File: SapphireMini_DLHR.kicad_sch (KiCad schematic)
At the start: 17 parts, among them IC201 DLHR-F50D-E1BD-C-NAV8, U201 LIS331DLHTR, U202 BMP390, U203 MS5525DSO

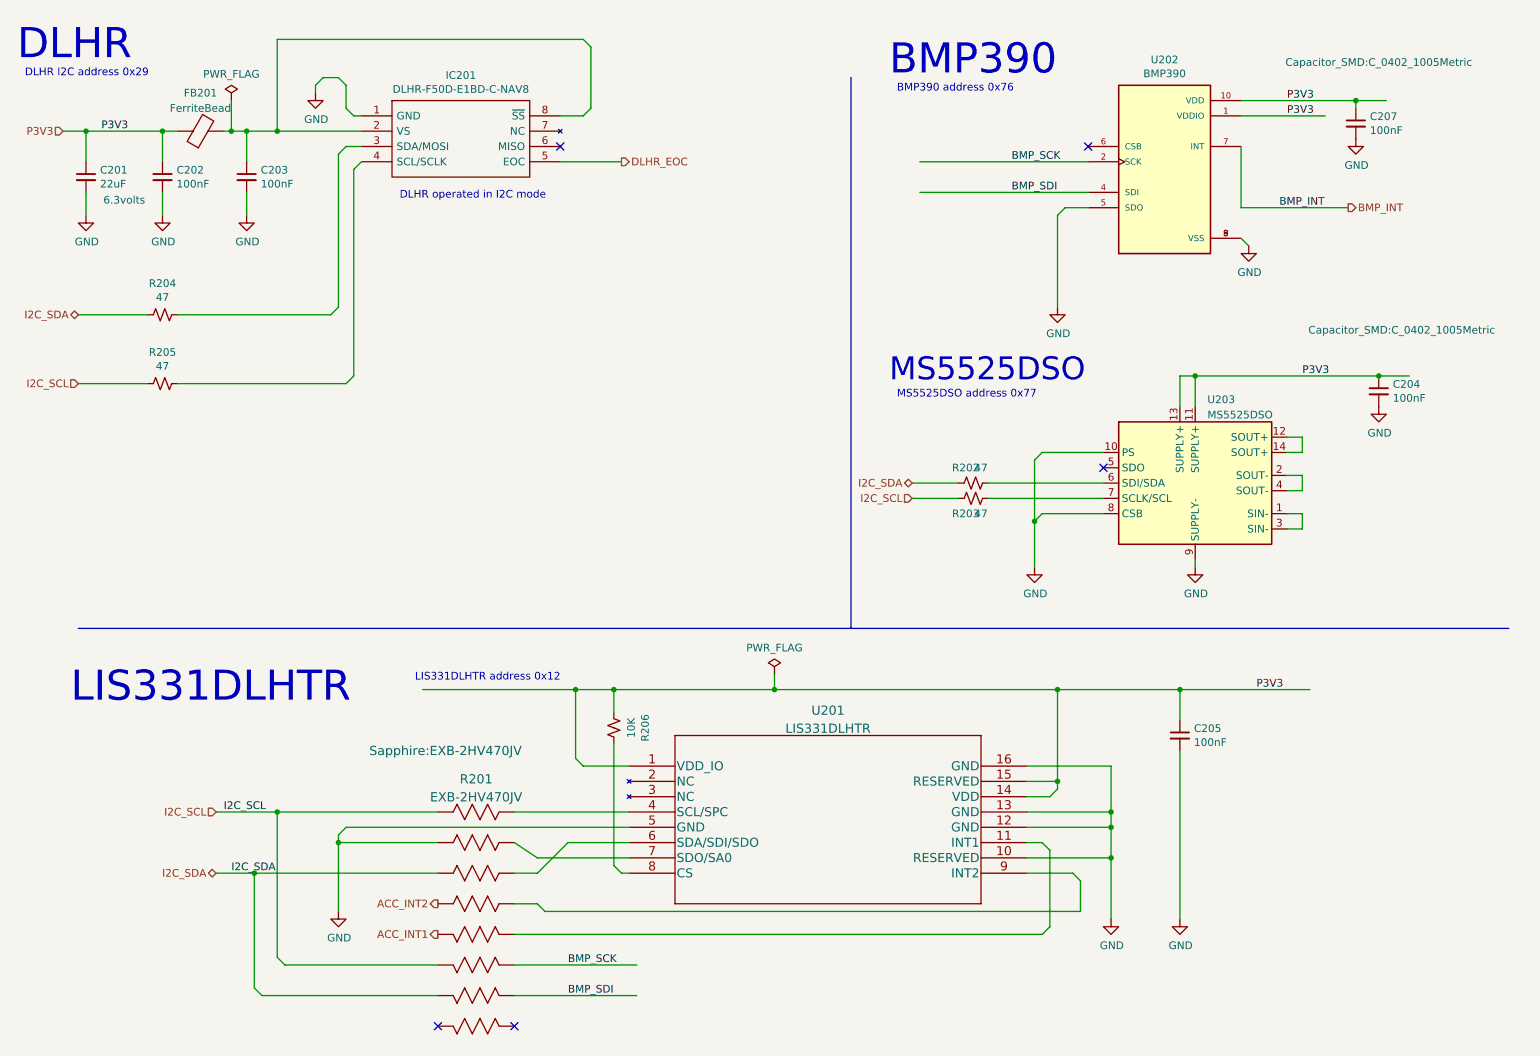
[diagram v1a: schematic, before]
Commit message: updated new layout - no routing
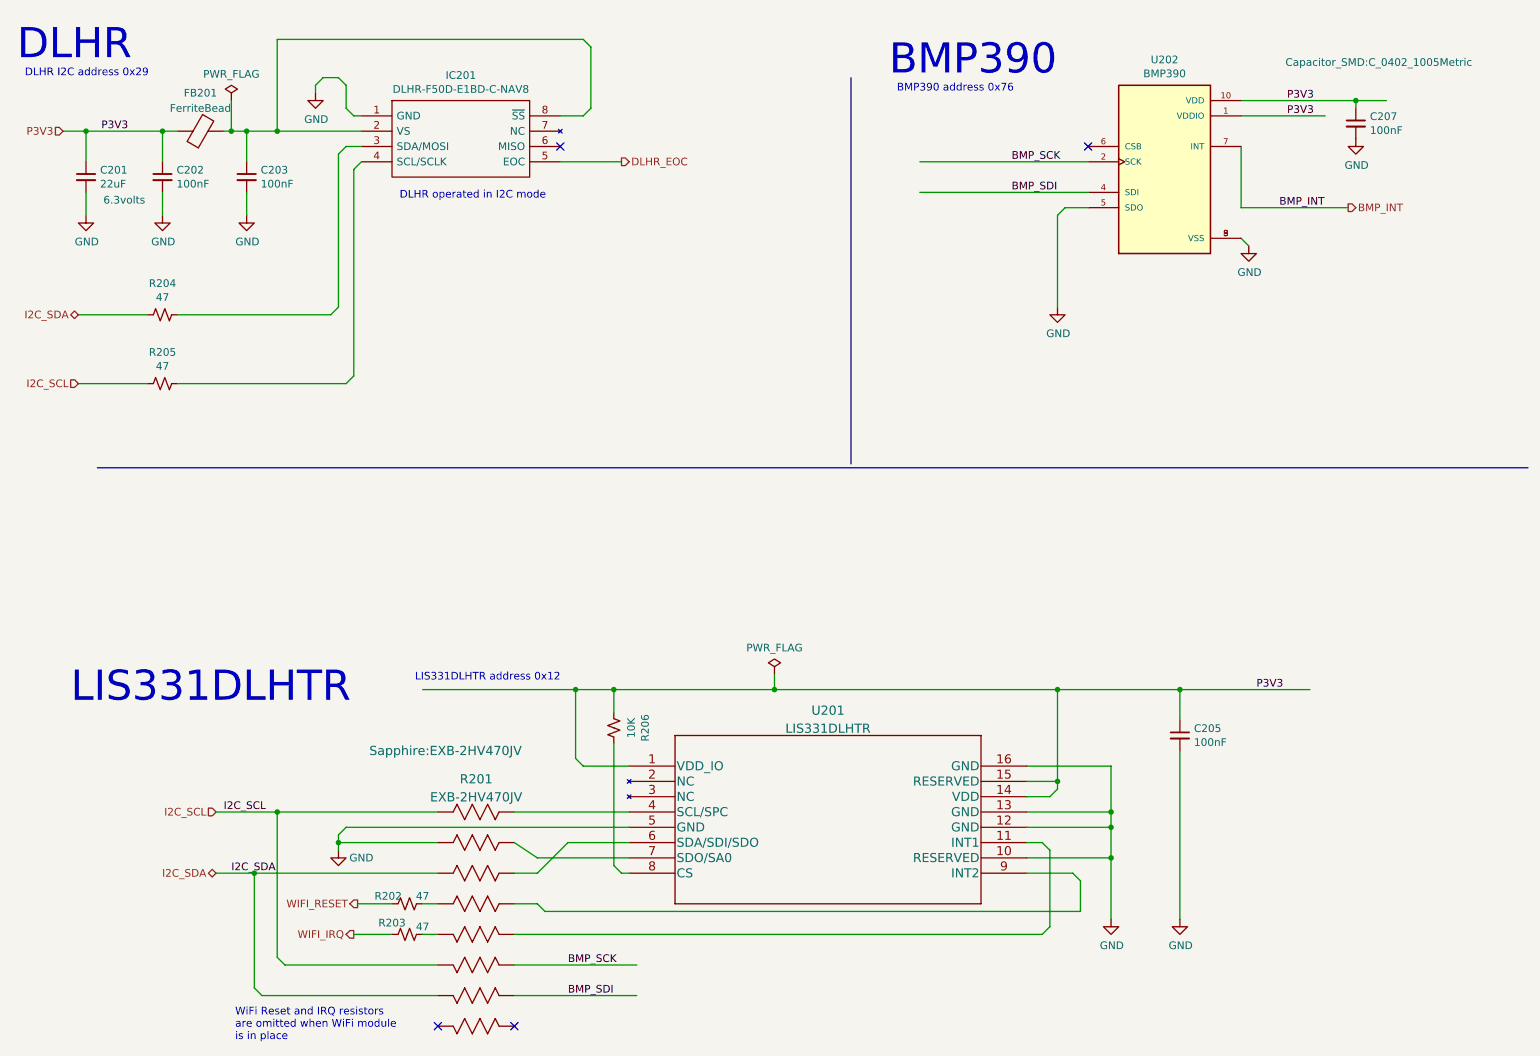
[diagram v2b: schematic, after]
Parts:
- removed C204: 100nF, Capacitor_SMD:C_0402_1005Metric, symbol Device:C_Small
- removed U203: MS5525DSO, Sapphire:TE_5525DSO-DB001DS, symbol Sensor_Pressure:MS5525DSO
- R201: symbol PanasonicRA:EXB-2HV470JV -> sapphireMini:EXB-2HV470JV_1
- U202: symbol BMP388:BMP388 -> sapphireMini:BMP388; MANUFACTURER (none) -> BOSCH
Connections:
- net ACC_INT1 is gone; now on an unnamed net: R201.5
- net ACC_INT2 is gone; now on an unnamed net: R201.4
- net I2C_SCL: no longer R203.2
- net I2C_SDA: no longer R202.2
- new net WIFI_IRQ: R203.2
- new net WIFI_RESET: R202.2
- no-connect marks 5 -> 4
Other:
- note added: "WiFi Reset and IRQ resistors are omitted when WiFi module is in place"
- note removed: "MS5525DSO"
- note removed: "MS5525DSO address 0x77"

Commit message: 6 Layer Routing
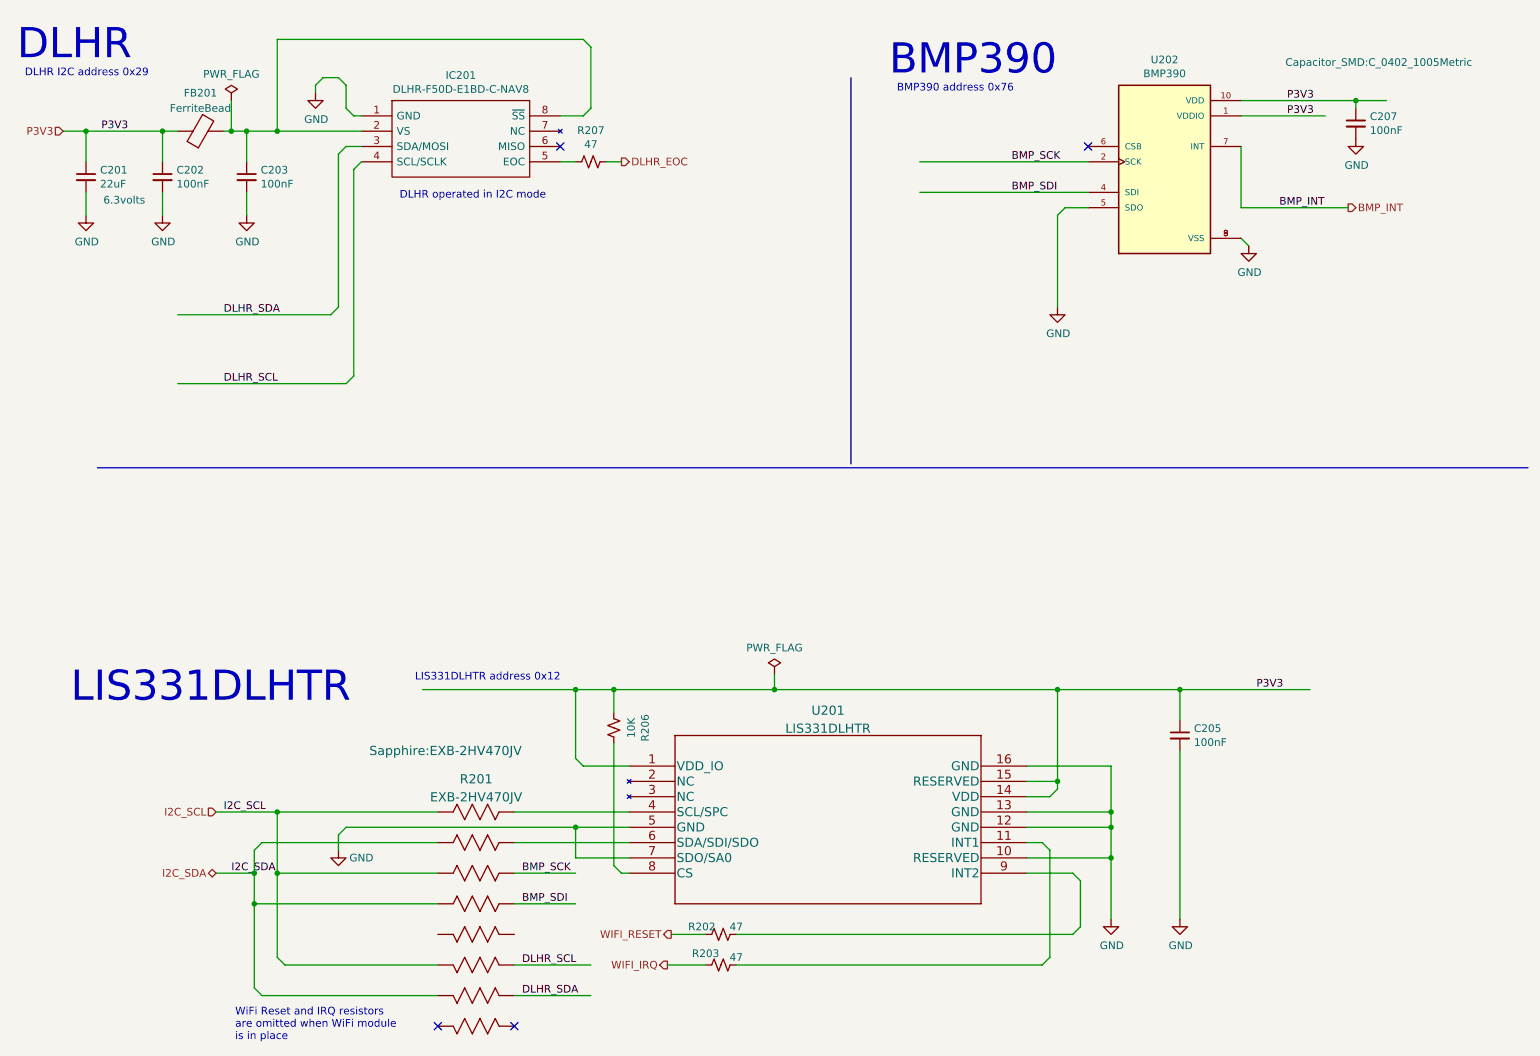
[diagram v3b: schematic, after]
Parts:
- removed R204, R205: 47, Resistor_SMD:R_0603_1608Metric, symbol Device:R_Small_US
- added R207: 47, Resistor_SMD:R_0603_1608Metric, symbol Device:R_Small_US
- FB201: footprint Inductor_SMD:L_0201_0603Metric -> Inductor_SMD:L_0603_1608Metric
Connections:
- net BMP_SCK: now also R201.14; no longer R201.11
- net BMP_SDI: now also R201.13; no longer R201.10
- net DLHR_EOC: now also R207.1; no longer IC201.5 (EOC)
- net GND: now also U201.7 (SDO/SA0); no longer R201.2
- net I2C_SCL: now also R201.3
- net I2C_SDA: now also R201.2, R201.4; no longer R201.3
- net DLHR_SDA: now reaches IC201.3 (SDA/MOSI)
- net DLHR_SDA: now also R201.10
- net DLHR_SCL: now reaches IC201.4 (SCL/SCLK)
- net DLHR_SCL: now also R201.11
- net at R201.12: no longer U201.11 (INT1)
- net at U201.9 (INT2): now also R202.1; no longer R201.13
- net at U201.6 (SDA/SDI/SDO): now also R201.15; no longer R201.14
- net at R201.5: no longer R203.1
- new net: IC201.5 (EOC), R207.2
- new net: R203.1, U201.11 (INT1)
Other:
- moved on the sheet: R202, R203

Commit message: Added optional RSCK footprint
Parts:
- C201: Attrition (none) -> 0
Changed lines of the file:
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@@
+      (effects (font (size 1.27 1.27)) hide)
+    )
+    (property "Attrition" "0" (id 17) (at 27.94 41.91 0)
       (effects (font (size 1.27 1.27)) hide)
     )

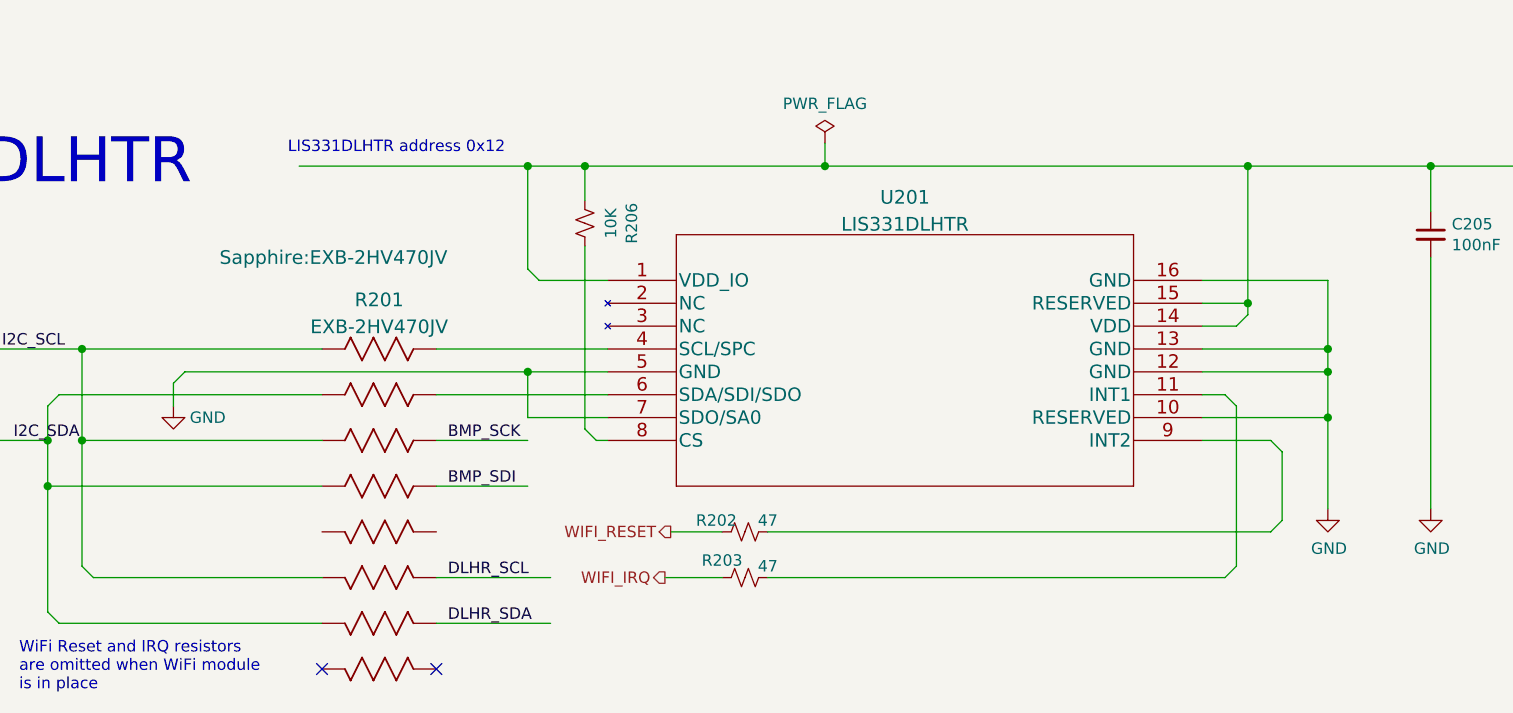
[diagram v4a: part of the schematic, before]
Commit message: Updated to fix noted problems
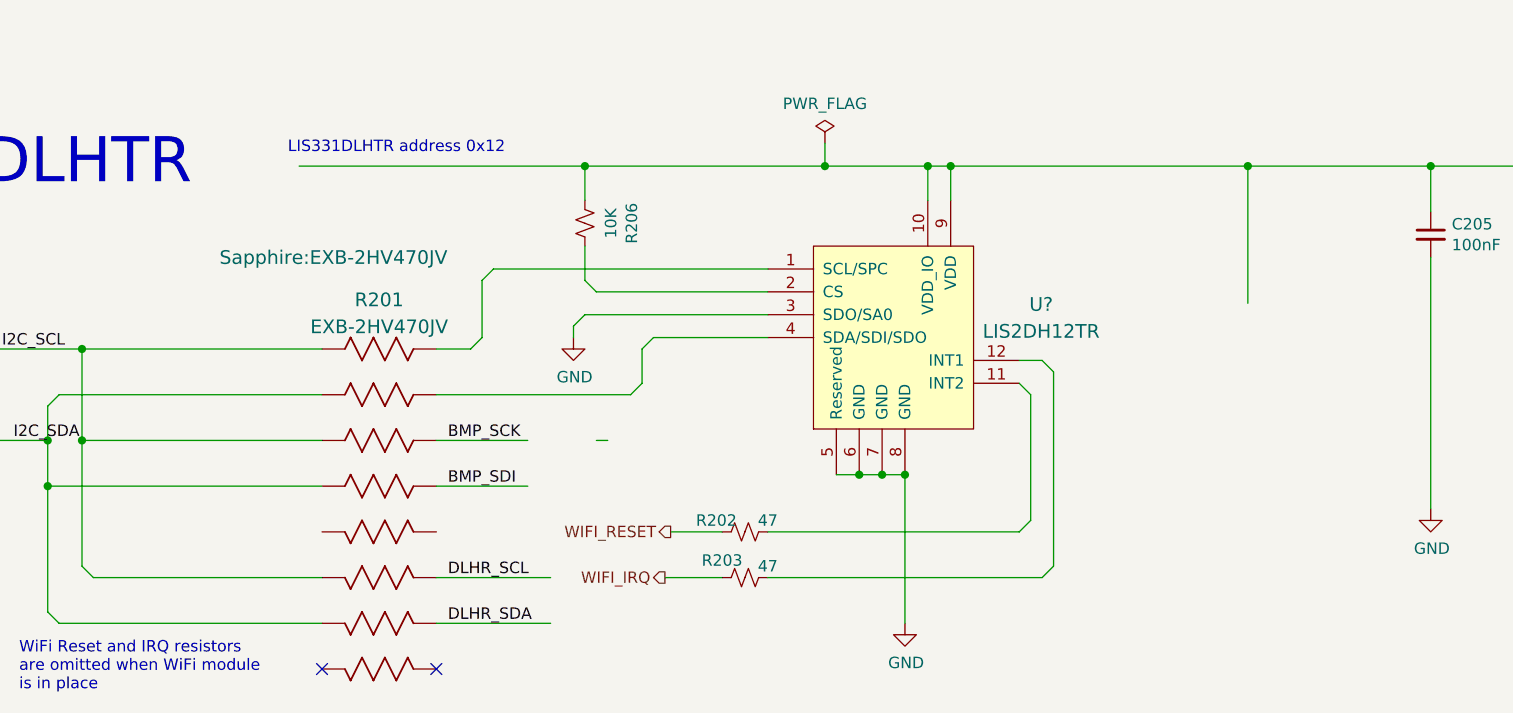
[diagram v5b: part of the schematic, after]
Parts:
- removed U201: LIS331DLHTR, Sapphire:LIS331DLHTR, symbol sapphireMini:LIS331DLHTR
- added U?: LIS2DH12TR, digikey-footprints:VFLGA-12_2x2mm, symbol dk_Motion-Sensors-Accelerometers:LIS2DH12TR
- IC201: footprint DLHRF50DE1BDCNAV8 -> Sapphire:DLHRF50DE1BDCNAV8
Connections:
- net GND: now also U?.3 (SDO/SA0), U?.5 (Reserved), U?.6 (GND), U?.7 (GND), U?.8 (GND)
- net P3V3: now also U?.10 (VDD_IO), U?.9 (VDD)
- net at R206.1: now also U?.2 (CS)
- net at R201.15: now also U?.4 (SDA/SDI/SDO)
- net at R201.16: now also U?.1 (SCL/SPC)
- net at R202.1: now also U?.11 (INT2)
- net at R203.1: now also U?.12 (INT1)

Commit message: InProgress
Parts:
- U202: footprint PQFN50P200X200X80-10N -> Sapphire:BMP388
- gave numbers to parts that had none: 1
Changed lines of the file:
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@@
     (property "Reference" "U202" (id 0) (at 207.01 22.4282 0))
     (property "Value" "BMP390" (id 1) (at 207.01 24.7396 0))
-    (property "Footprint" "PQFN50P200X200X80-10N" (id 2) (at 207.01 41.91 0)
+    (property "Footprint" "Sapphire:BMP388" (id 2) (at 207.01 41.91 0)
       (effects (font (size 1.27 1.27)) (justify left bottom) hide)
     )
@@
   (symbol (lib_id "dk_Motion-Sensors-Accelerometers:LIS2DH12TR") (at 151.13 146.05 0) (unit 1)
     (in_bom yes) (on_board yes) (fields_autoplaced)
-    (property "Reference" "U?" (id 0) (at 166.2657 142.3722 0)
+    (property "Reference" "U201" (id 0) (at 166.2657 142.3722 0)
       (effects (font (size 1.524 1.524)))
     )
@@
   (symbol (lib_id "power:GND") (at 151.13 177.8 0) (unit 1)
     (in_bom yes) (on_board yes)
-    (property "Reference" "#PWR?" (id 0) (at 151.13 184.15 0)
+    (property "Reference" "#PWR0109" (id 0) (at 151.13 184.15 0)
       (effects (font (size 1.27 1.27)) hide)
     )
@@
   (symbol (lib_id "power:GND") (at 114.3 146.05 0) (unit 1)
     (in_bom yes) (on_board yes)
-    (property "Reference" "#PWR?" (id 0) (at 114.3 152.4 0)
-      (effects (font (size 1.27 1.27)) hide)
-    )
+    (property "Reference" "#PWR0110" (id 0) (at 114.3 152.4 0)
+      (effects (font (size 1.27 1.27)) hide)
+    )

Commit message: M2R2 basic DRC passed
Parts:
- U201: footprint digikey-footprints:VFLGA-12_2x2mm -> Sapphire:LIS2DH12TR
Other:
- note added: "LIS2DH12TR"
- note removed: "LIS331DLHTR"
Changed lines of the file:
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@@
     (effects (font (size 1.27 1.27)) (justify left bottom))
   )
-  (text "LIS331DLHTR" (at 25.4 129.54 0)
+  (text "LIS2DH12TR" (at 39.37 107.95 0)
     (effects (font (size 5 5)) (justify left bottom))
   )
@@
       (effects (font (size 1.524 1.524)))
     )
-    (property "Footprint" "digikey-footprints:VFLGA-12_2x2mm" (id 2) (at 156.21 140.97 0)
+    (property "Footprint" "Sapphire:LIS2DH12TR" (id 2) (at 156.21 140.97 0)
       (effects (font (size 1.524 1.524)) (justify left) hide)
     )

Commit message: Design R2 sent to OSH Park
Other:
- note added: "or LIS2HH12TR"
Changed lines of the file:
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@@
     (effects (font (size 1.27 1.27)) (justify left bottom))
+  )
+  (text "or LIS2HH12TR" (at 48.26 115.57 0)
+    (effects (font (size 5 5)) (justify left bottom))
   )
   (text "DLHR operated in I2C mode" (at 80.01 45.72 0)
